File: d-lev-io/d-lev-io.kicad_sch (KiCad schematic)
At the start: 10 parts, among them J1 PJ-059A, J3 USB_C_Receptacle_USB2.0, J4 AudioJack3, J5 DIN-41524, U4 AMS1117-5.0, U5 TPS54336ADDA

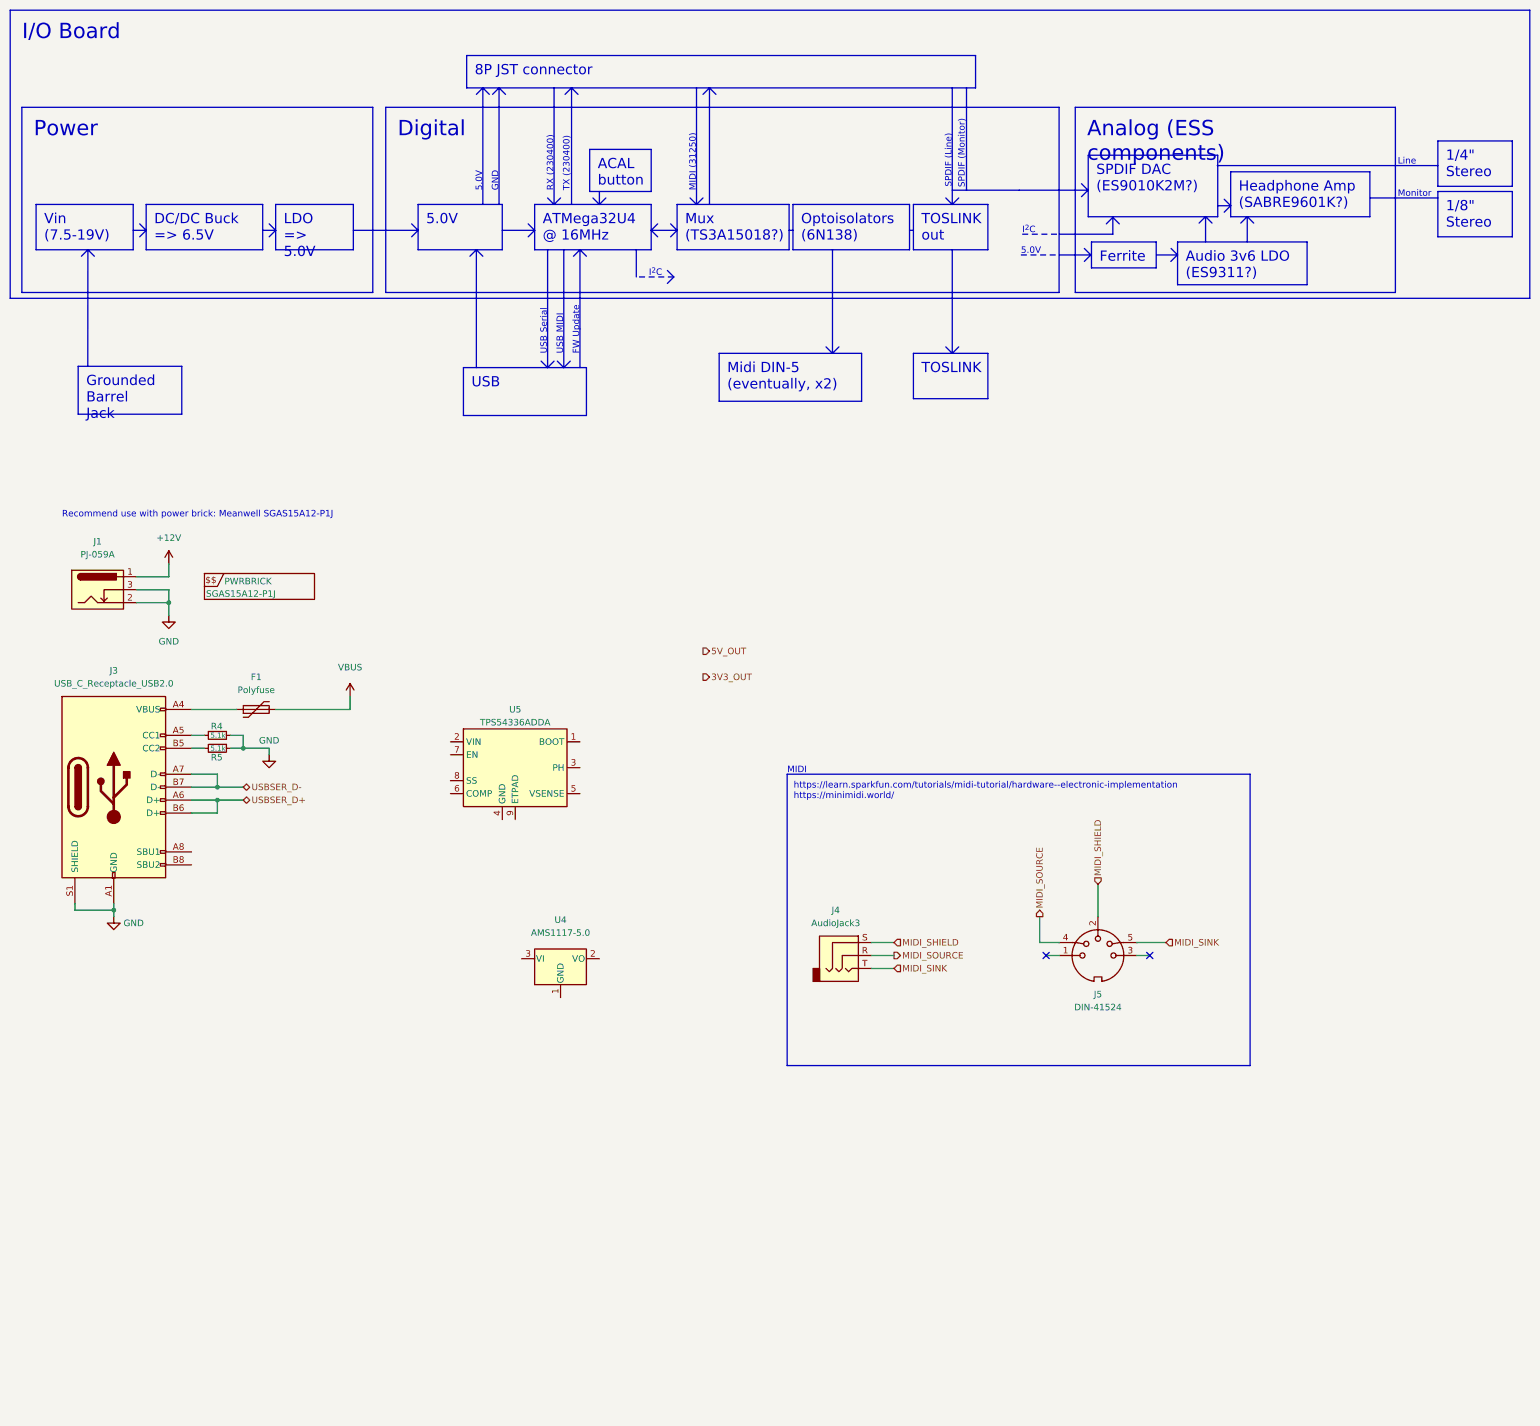
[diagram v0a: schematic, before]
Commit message: Many changes
Reorganized libraries to share between projects
Set up JLC 2- and 4- layer design rules
Finished copying over most of the schematic (excluding I/O board)
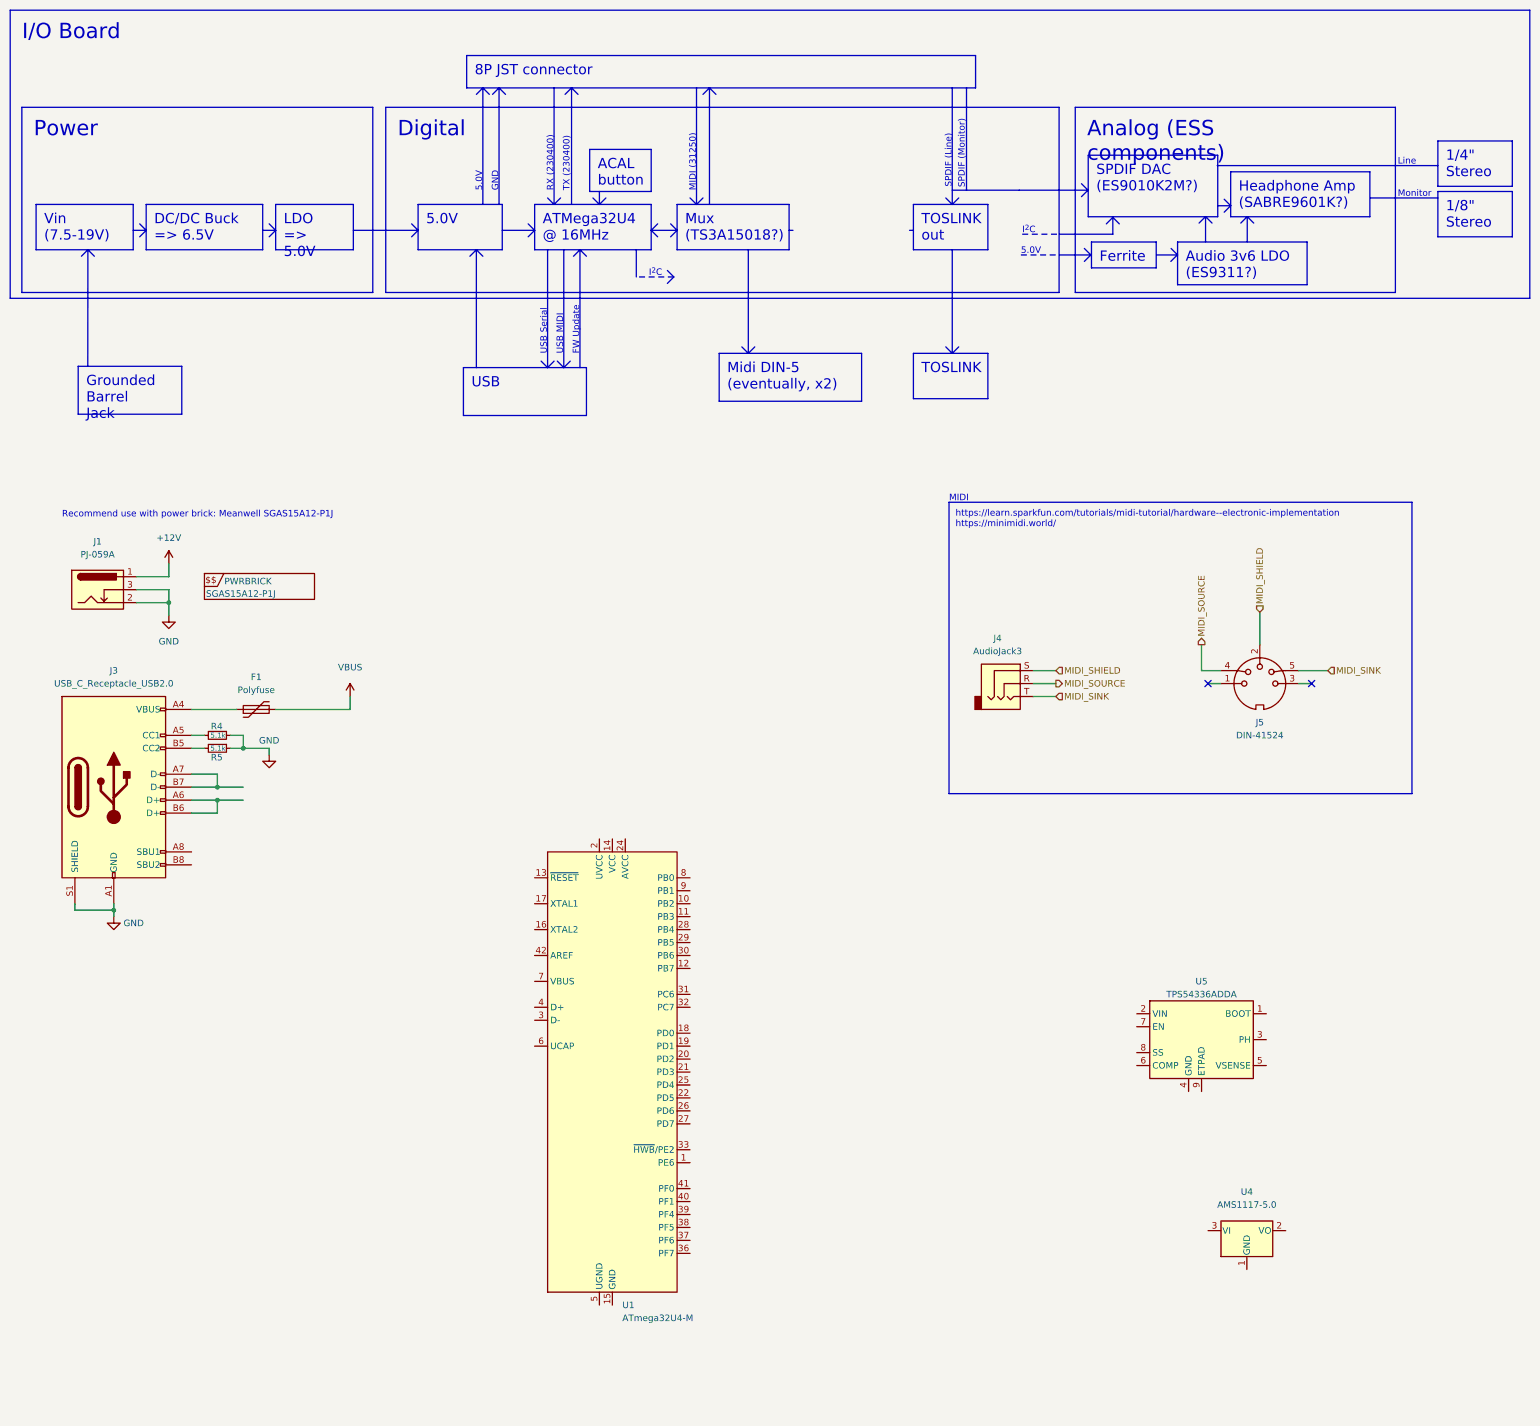
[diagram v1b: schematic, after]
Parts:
- added U1: ATmega32U4-M, Package_DFN_QFN:QFN-44-1EP_7x7mm_P0.5mm_EP5.2x5.2mm, symbol MCU_Microchip_ATmega:ATmega32U4-M
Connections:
- net USBSER_D+: no longer names the net of J3.A6 (D+), J3.B6 (D+)
- net USBSER_D-: no longer names the net of J3.A7 (D-), J3.B7 (D-)
- new net: U1.14 (VCC), U1.34 (VCC)
- new net: U1.15 (GND), U1.23 (GND), U1.35 (GND), U1.43 (GND), U1.45 (GND)
- new net: U1.24 (AVCC), U1.44 (AVCC)
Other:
- moved on the sheet: J4, J5, U4, U5

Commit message: Reorganized, and updates
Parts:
- added U2: AMS1117-5.0, Package_TO_SOT_SMD:SOT-223-3_TabPin2, symbol Regulator_Linear:AMS1117-5.0
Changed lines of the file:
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@@
+    )
+  )
+  (symbol (lib_name "AMS1117-5.0_1") (lib_id "Regulator_Linear:AMS1117-5.0") (at 144.78 60.96 0) (unit 1)
+    (in_bom yes) (on_board yes) (dnp no) (fields_autoplaced)
+    (property "Reference" "U2" (at 144.78 54.61 0)
+      (effects (font (size 1.27 1.27)))
+    )
+    (property "Value" "AMS1117-5.0" (at 144.78 57.15 0)
+      (effects (font (size 1.27 1.27)))
+    )
+    (property "Footprint" "Package_TO_SOT_SMD:SOT-223-3_TabPin2" (at 144.78 55.88 0)
+      (effects (font (size 1.27 1.27)) hide)
+    )
+    (property "Datasheet" "http://www.advanced-monolithic.com/pdf/ds1117.pdf" (at 147.32 67.31 0)
+      (effects (font (size 1.27 1.27)) hide)
+    )
+    (pin "1")
+    (pin "2")
+    (pin "3")
+    (instances
+      (project "d-lev-io"
+        (path "/9261a07b-ae4a-4d72-8042-ea097cd0e5ed"
+          (reference "U2") (unit 1)
+        )
+      )
     )
   )

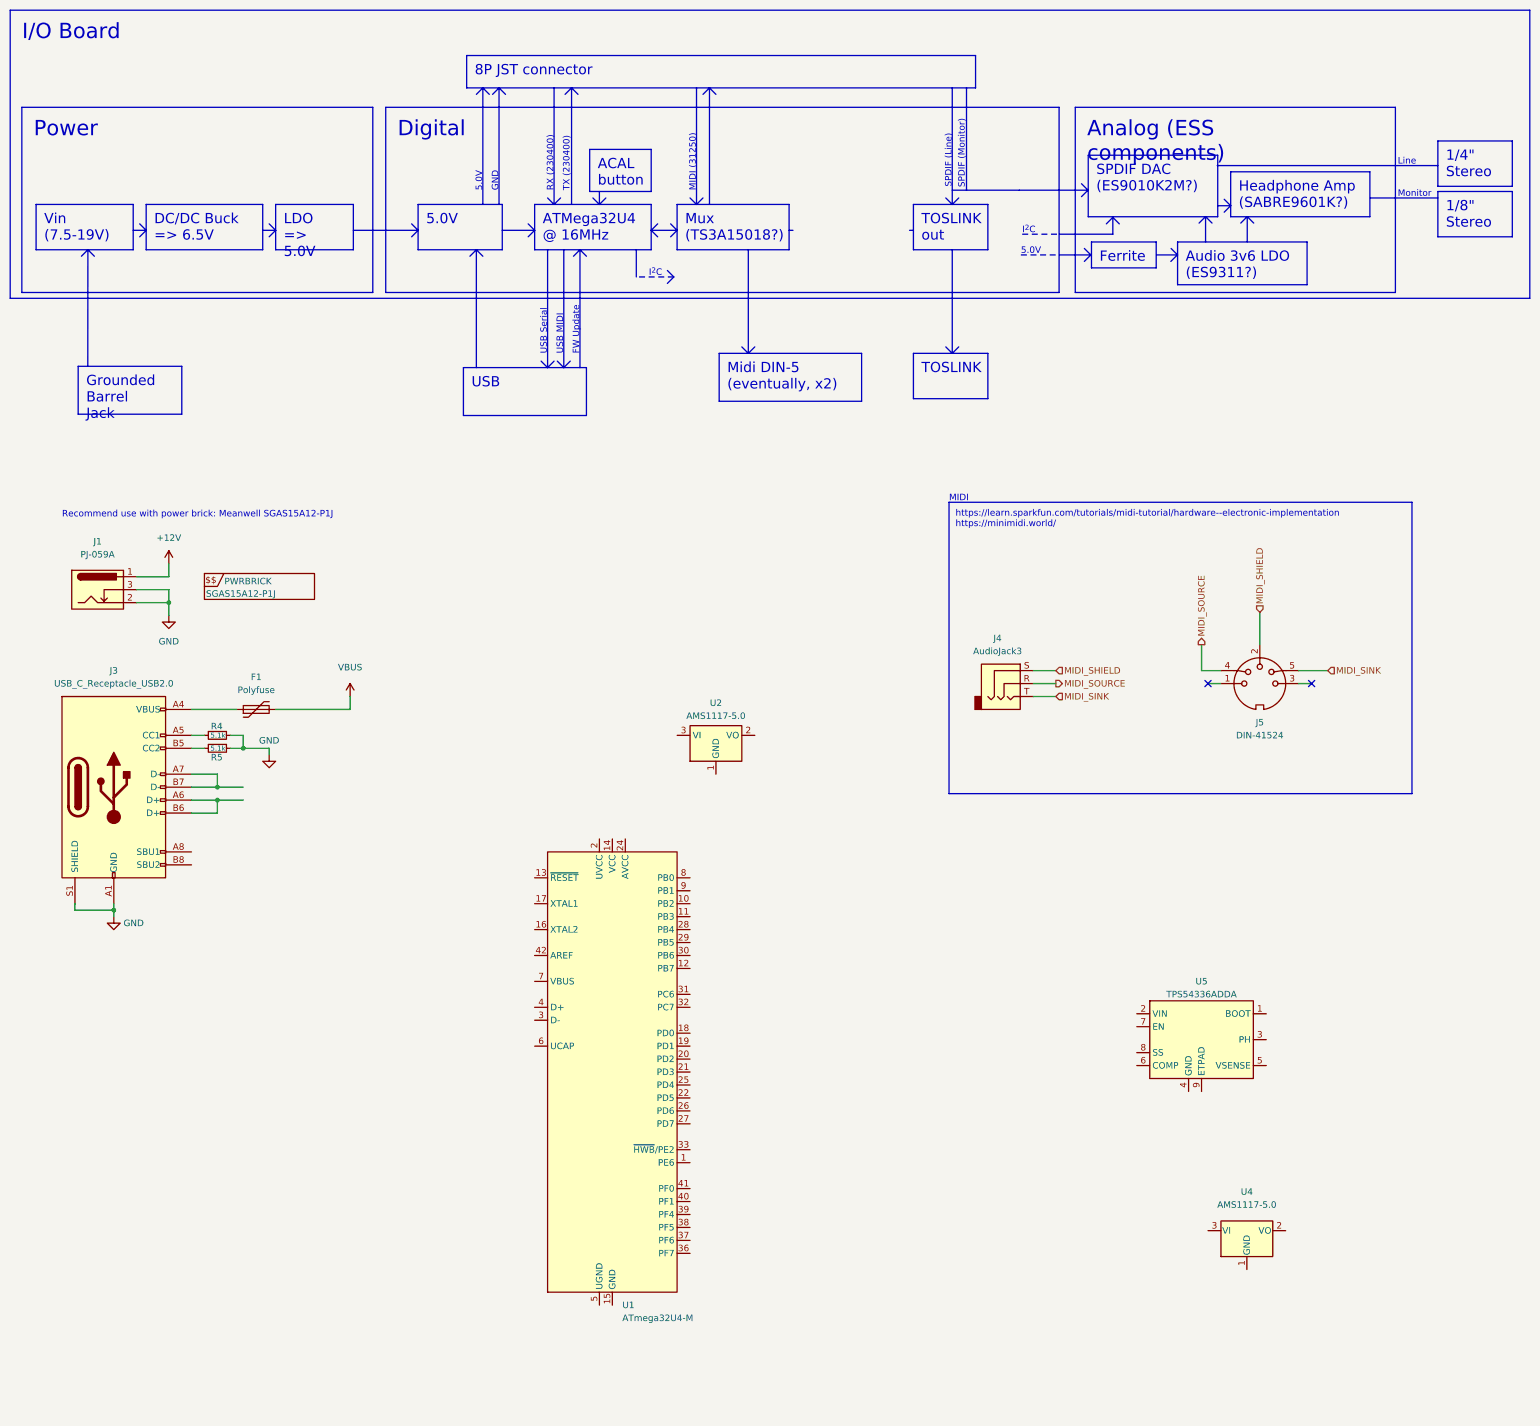
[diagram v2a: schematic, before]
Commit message: schematic + wiring for avr
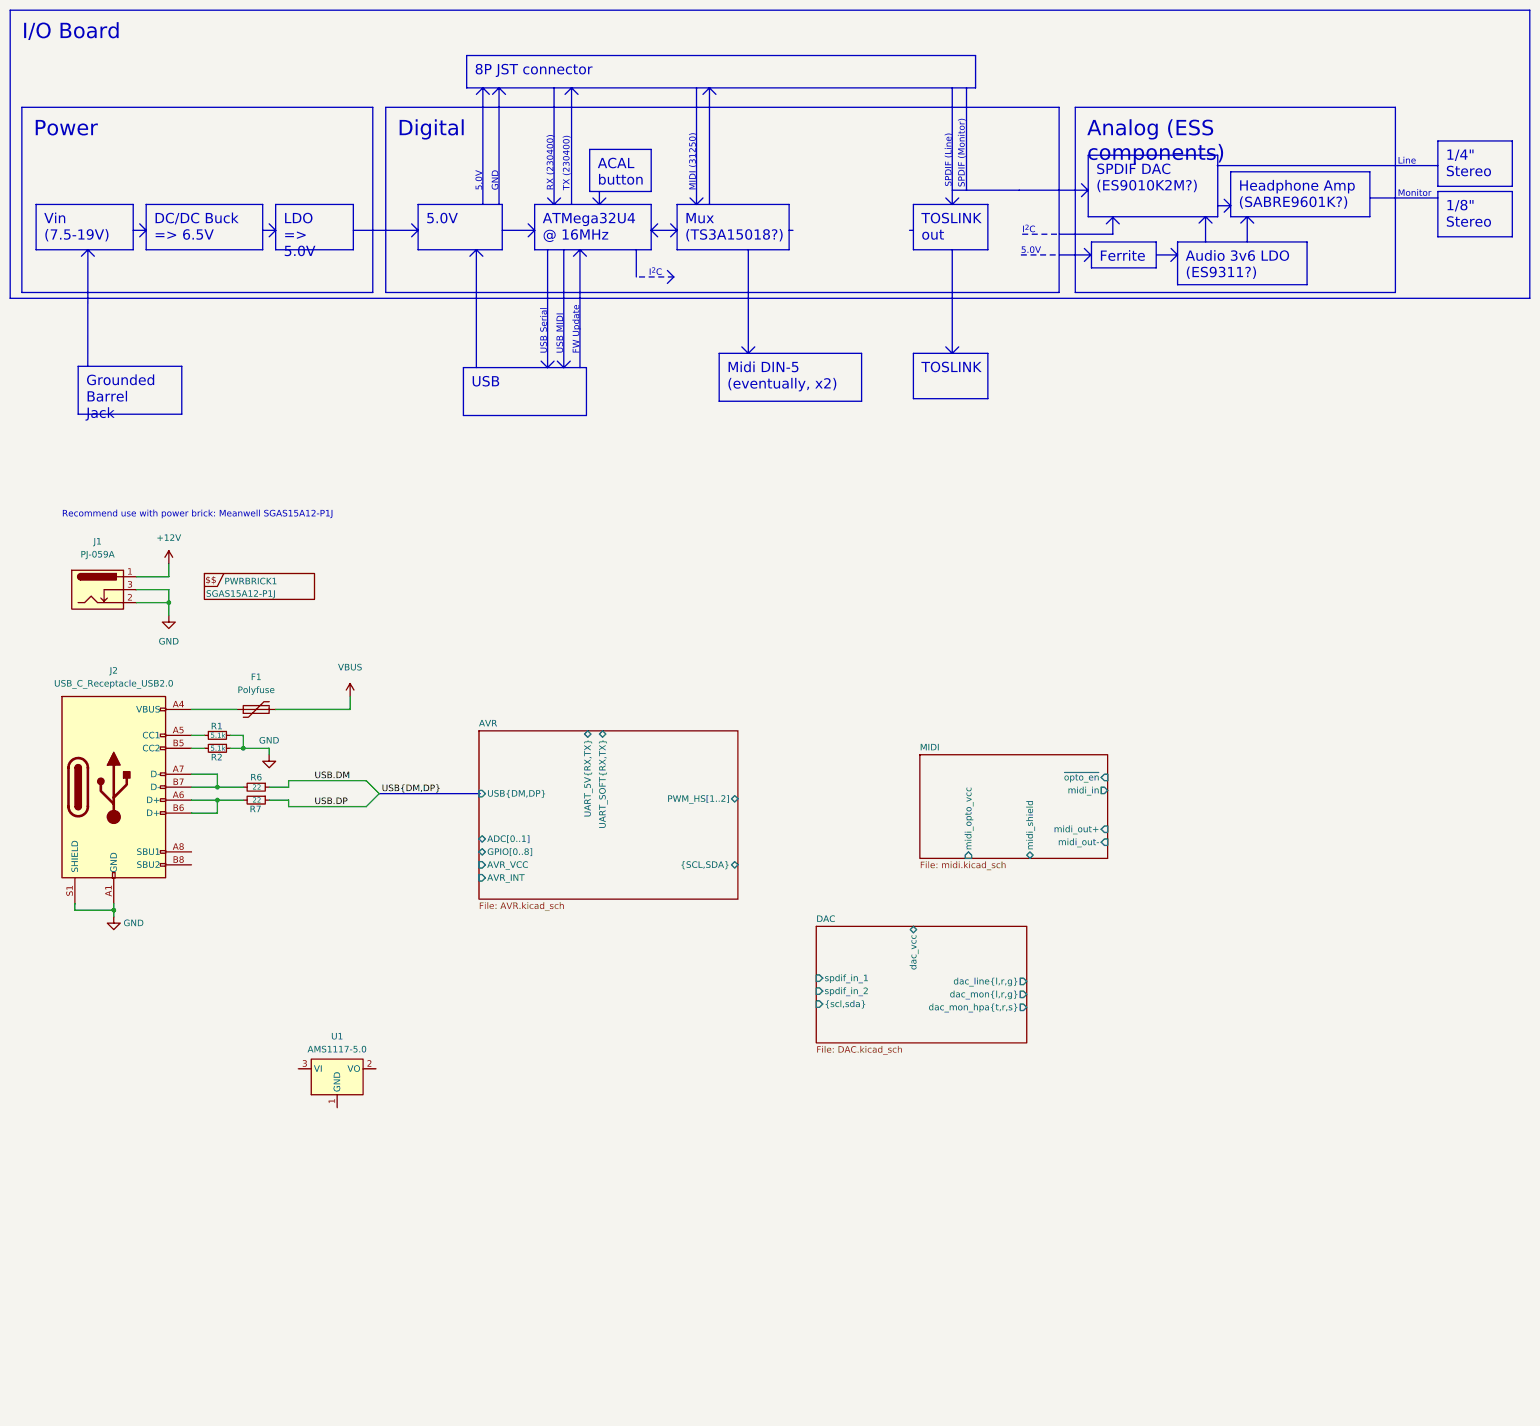
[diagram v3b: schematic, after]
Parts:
- removed J4: AudioJack3, symbol Connector:AudioJack3
- removed J5: DIN-41524, symbol Connector:DIN-5_180degree
- removed U1: ATmega32U4-M, Package_DFN_QFN:QFN-44-1EP_7x7mm_P0.5mm_EP5.2x5.2mm, symbol MCU_Microchip_ATmega:ATmega32U4-M
- removed U4: AMS1117-5.0, Package_TO_SOT_SMD:SOT-223-3_TabPin2, symbol Regulator_Linear:AMS1117-5.0
- removed U5: TPS54336ADDA, Package_SO:TI_SO-PowerPAD-8_ThermalVias, symbol Regulator_Switching:TPS54336ADDA
- added R6, R7: 22, Resistor_SMD:R_0805_2012Metric_Pad1.20x1.40mm_HandSolder, symbol Device:R_Small
- renumbered J3 to J2, PWRBRICK to PWRBRICK1, R4 to R1, R5 to R2, U2 to U1
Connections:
- net at J2.A6 (D+), J2.B6 (D+): now also R7.2
- net at J2.A7 (D-), J2.B7 (D-): now also R6.2
- new net USB.DM: R6.1
- new net USB.DP: R7.1
- no-connect marks 2 -> 0
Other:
- added sheet AVR (AVR.kicad_sch)
- added sheet DAC (DAC.kicad_sch)
- added sheet MIDI (midi.kicad_sch)
- note removed: "MIDI"
- note removed: "https://learn.sparkfun.com/tutorials/midi-tutorial/hardware--electronic-implementation https://minimidi.world/"
- moved on the sheet: U1
